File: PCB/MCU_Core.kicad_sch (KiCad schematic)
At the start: 1 part, among them IC2 STM32F407IGT6

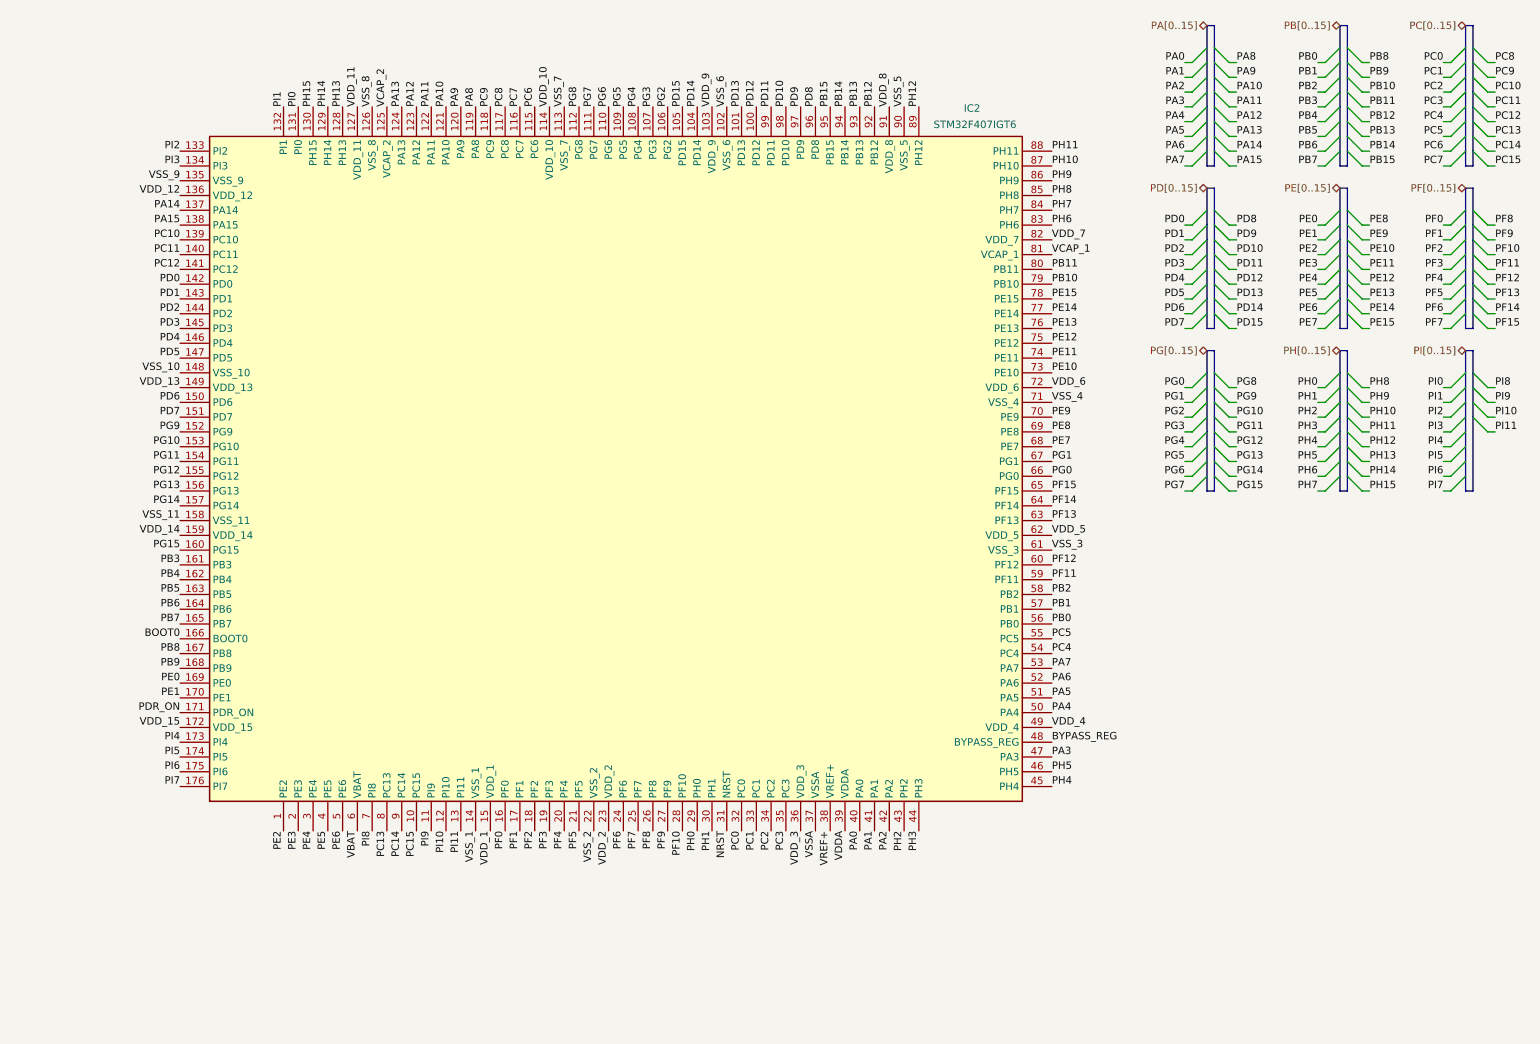
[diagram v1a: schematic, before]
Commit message: ADD supplies to UC
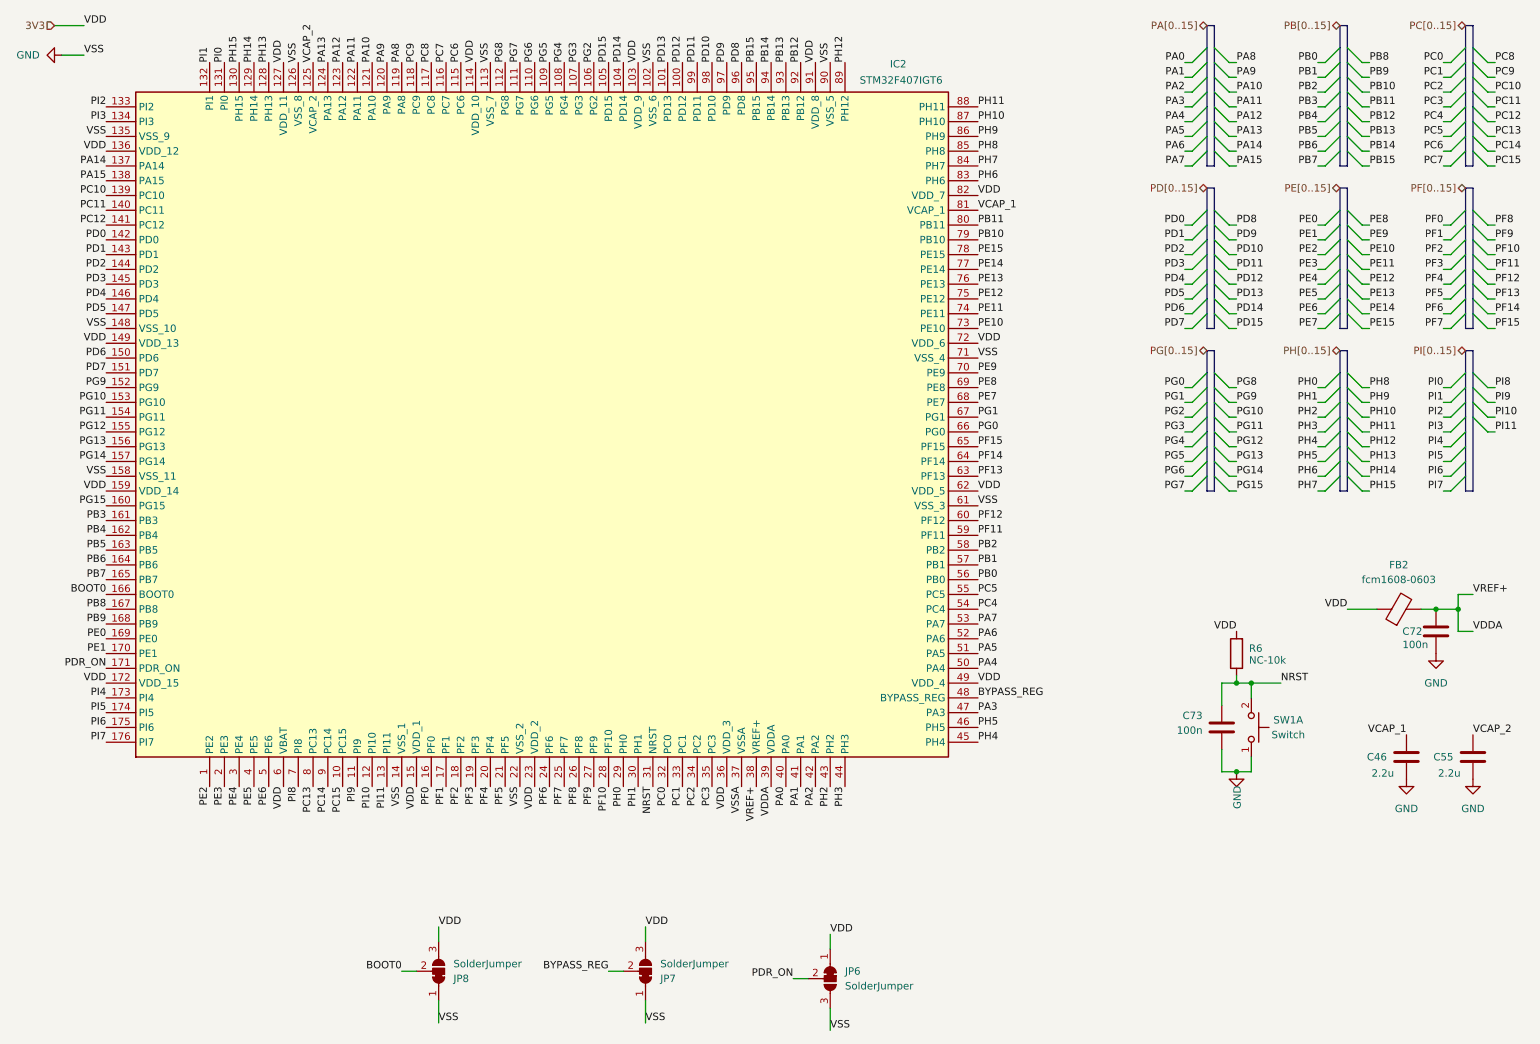
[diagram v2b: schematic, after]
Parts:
- added C46, C55: 2.2u, symbol Device:C
- added C72: 100n, symbol Device:C
- added C73: 100n, Capacitor_SMD:C_0603_1608Metric_Pad1.08x0.95mm_HandSolder, symbol Device:C
- added FB2: fcm1608-0603, symbol Device:FerriteBead
- added JP6, JP7, JP8: SolderJumper, Jumper:SolderJumper-3_P1.3mm_Bridged12_RoundedPad1.0x1.5mm, symbol Jumper:SolderJumper_3_Bridged12
- added R6: NC-10k, Resistor_SMD:R_0603_1608Metric_Pad0.98x0.95mm_HandSolder, symbol Device:R
- added SW1: Switch, SamacSys_Parts:KMR231NGLFS, symbol Switch:SW_Push_Dual_x2
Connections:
- net VDD_1 is gone; now on net 3V3: IC2.15 (VDD_1)
- net VDD_10 is gone; now on net 3V3: IC2.114 (VDD_10)
- net VDD_11 is gone; now on net 3V3: IC2.127 (VDD_11)
- net VDD_12 is gone; now on net 3V3: IC2.136 (VDD_12)
- net VDD_13 is gone; now on net 3V3: IC2.149 (VDD_13)
- net VDD_14 is gone; now on net 3V3: IC2.159 (VDD_14)
- net VDD_15 is gone; now on net 3V3: IC2.172 (VDD_15)
- net VDD_2 is gone; now on net 3V3: IC2.23 (VDD_2)
- net VDD_3 is gone; now on net 3V3: IC2.36 (VDD_3)
- net VDD_4 is gone; now on net 3V3: IC2.49 (VDD_4)
- net VDD_5 is gone; now on net 3V3: IC2.62 (VDD_5)
- net VDD_6 is gone; now on net 3V3: IC2.72 (VDD_6)
- net VDD_7 is gone; now on net 3V3: IC2.82 (VDD_7)
- net VDD_8 is gone; now on net 3V3: IC2.91 (VDD_8)
- net VDD_9 is gone; now on net 3V3: IC2.103 (VDD_9)
- net VREF+ is gone; now on net VDDA: IC2.38 (VREF+)
- net VSS_10 is gone; now on net GND: IC2.148 (VSS_10)
- net VSS_11 is gone; now on net GND: IC2.158 (VSS_11)
- net VSS_2 is gone; now on net GND: IC2.22 (VSS_2)
- net VSS_3 is gone; now on net GND: IC2.61 (VSS_3)
- net VSS_4 is gone; now on net GND: IC2.71 (VSS_4)
- net VSS_5 is gone; now on net GND: IC2.90 (VSS_5)
- net VSS_6 is gone; now on net GND: IC2.102 (VSS_6)
- net VSS_7 is gone; now on net GND: IC2.113 (VSS_7)
- net VSS_8 is gone; now on net GND: IC2.126 (VSS_8)
- net VSS_9 is gone; now on net GND: IC2.135 (VSS_9)
- net BOOT0: now also JP8.2 (C)
- net BYPASS_REG: now also JP7.2 (C)
- net NRST: now also C73.2, R6.1, SW1.2 (D)
- net PDR_ON: now also JP6.2 (C)
- net VCAP_1: now also C46.1
- net VCAP_2: now also C55.1
- net VDDA: now also C72.1, FB2.2
- net VBAT renamed 3V3
- net 3V3: now also FB2.1, JP6.1 (A), JP7.3 (B), JP8.3 (B), R6.2
- net VSS_1 renamed GND
- net GND: now also C46.2, C55.2, C72.2, C73.1, JP6.3 (B), JP7.1 (A), JP8.1 (A), SW1.1 (C)
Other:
- moved on the sheet: IC2

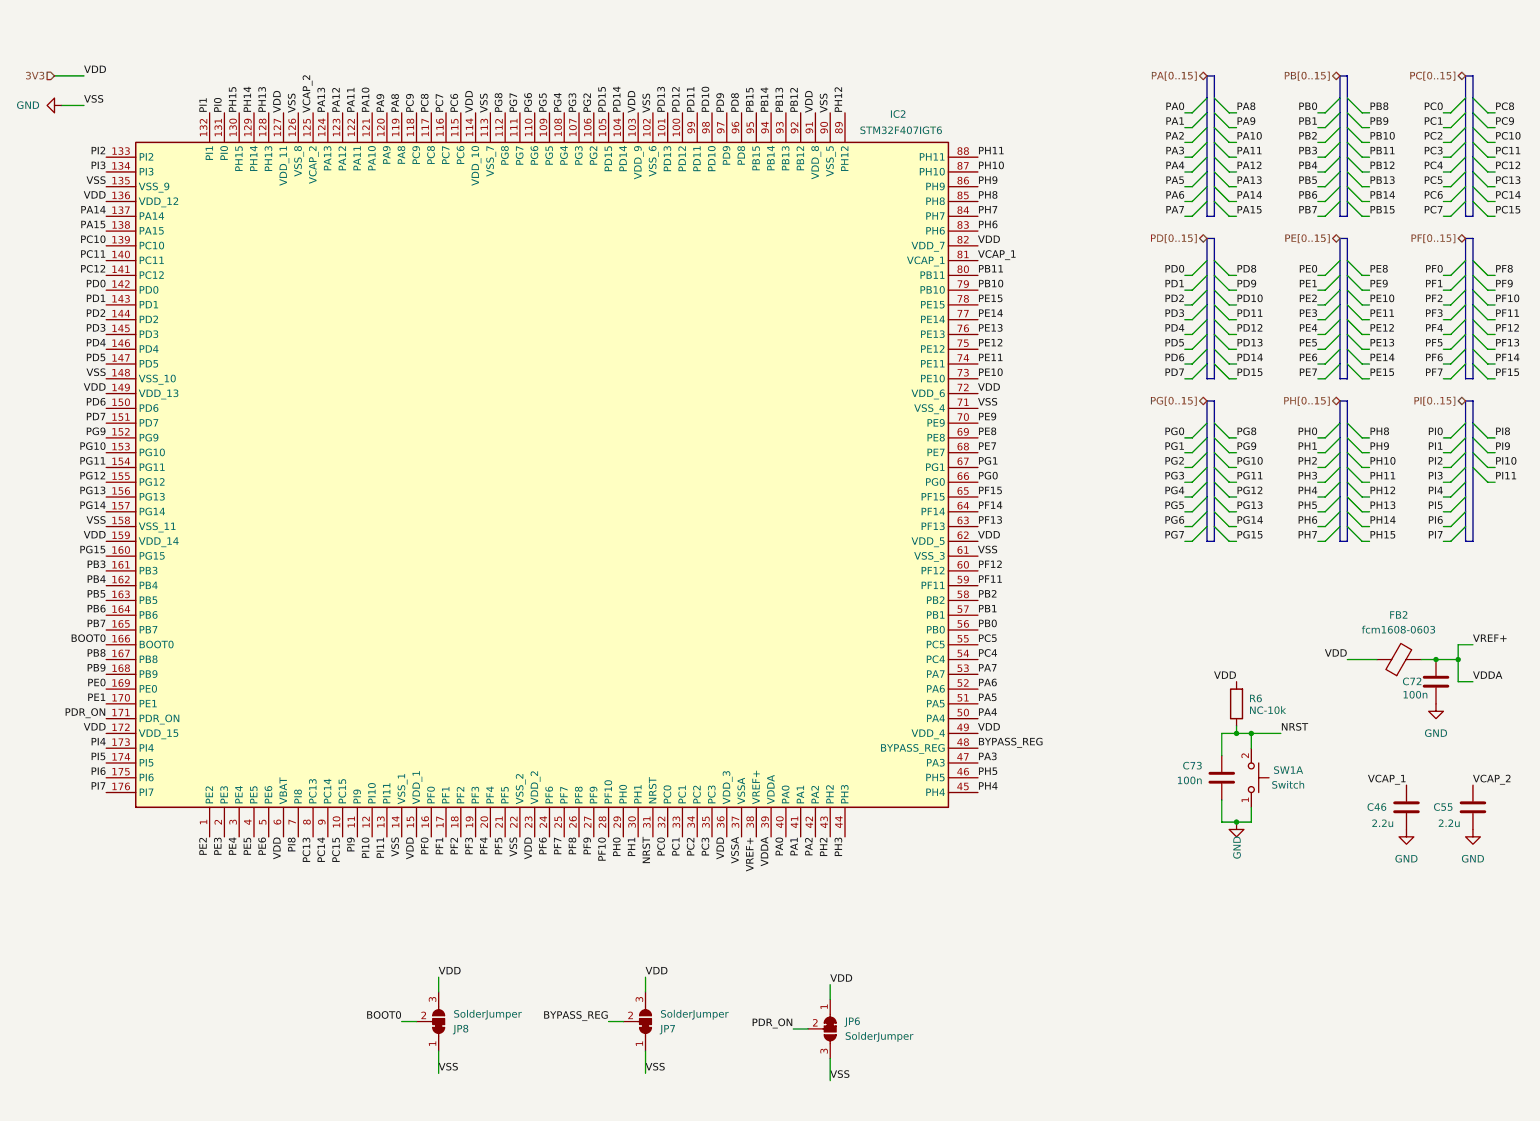
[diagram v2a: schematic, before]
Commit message: Updated MCU sheet
Added decoupling capacitors
Linked Ethernet to MCU
Started Usb linking to MCU
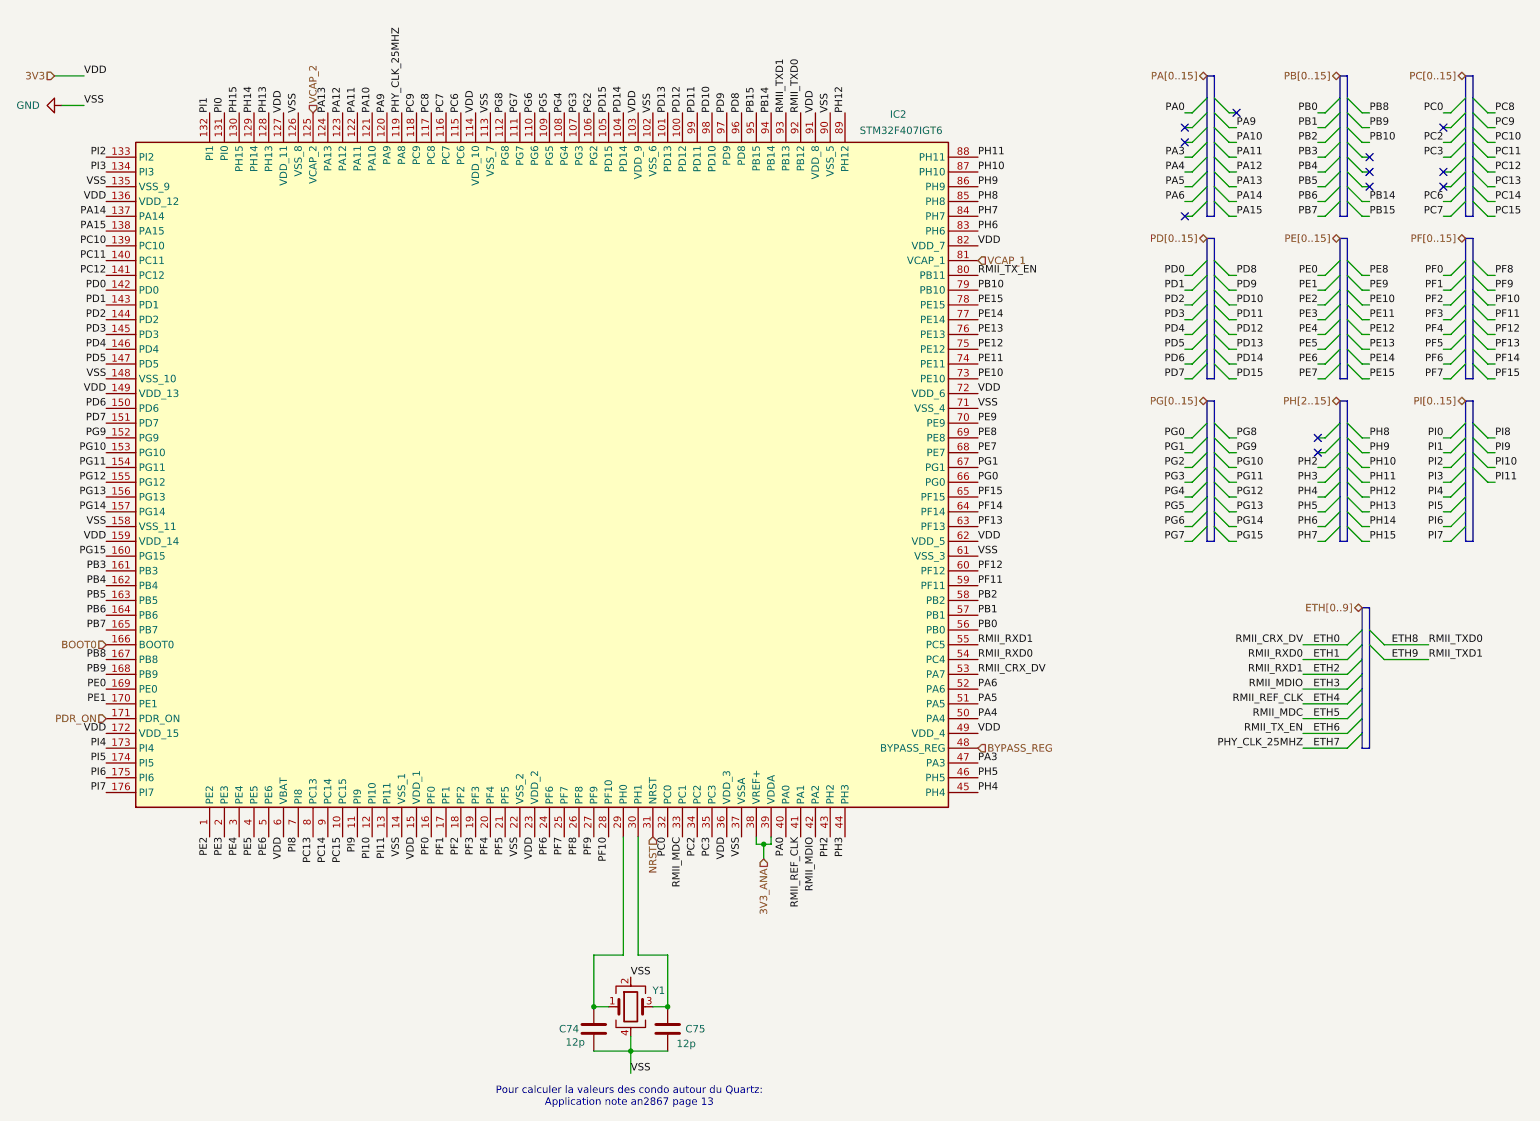
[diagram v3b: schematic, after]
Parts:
- removed C46, C55: 2.2u, symbol Device:C
- removed C72: 100n, symbol Device:C
- removed C73: 100n, Capacitor_SMD:C_0603_1608Metric_Pad1.08x0.95mm_HandSolder, symbol Device:C
- removed FB2: fcm1608-0603, symbol Device:FerriteBead
- removed JP6, JP7, JP8: SolderJumper, Jumper:SolderJumper-3_P1.3mm_Bridged12_RoundedPad1.0x1.5mm, symbol Jumper:SolderJumper_3_Bridged12
- removed R6: NC-10k, Resistor_SMD:R_0603_1608Metric_Pad0.98x0.95mm_HandSolder, symbol Device:R
- removed SW1: Switch, SamacSys_Parts:KMR231NGLFS, symbol Switch:SW_Push_Dual_x2
- added C74, C75: 12p, Capacitor_SMD:C_0603_1608Metric_Pad1.08x0.95mm_HandSolder, symbol Device:C
- added Y1: Crystal_GND24, symbol Device:Crystal_GND24
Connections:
- net VSSA is gone; now on net GND: IC2.37 (VSSA)
- net GND: now also C74.2, C75.2, Y1.2, Y1.4
- net PA1 renamed ETH4
- net PA2 renamed ETH3
- net PA7 renamed ETH0
- net PA8 renamed ETH7
- net PB11 renamed ETH6
- net PB12 renamed ETH8
- net PB13 renamed ETH9
- net PC1 renamed ETH5
- net PC4 renamed ETH1
- net PC5 renamed ETH2
- net PH0: no longer names the net of IC2.29 (PH0)
- net PH0: now also C74.1, Y1.1
- net PH1: no longer names the net of IC2.30 (PH1)
- net PH1: now also C75.1, Y1.3
- net VDDA renamed 3V3_ANA
- no-connect marks 0 -> 12
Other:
- note added: "Pour calculer la valeurs des condo autour du Quartz: Application note an2867 page 13"

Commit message: Updated a lot of stuff:
Added encoders,
Added 5V power supply for actuators
Added 12V power supply for actuators
Renamed sheets to be clearer
Added usb debug
Modify MCU sheet to be A3 format
Linked some pins
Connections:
- net PG11 is gone; now on net ETH6: IC2.154 (PG11)
- net ETH6: no longer IC2.80 (PB11)
- net PA0 renamed SERVO3
- net PA10 renamed RX_UC
- net PA11 renamed D-
- net PA12 renamed D+
- net PA3 renamed CurrentSenseMotor1
- net PA4 renamed CurrentSenseMotor2
- net PA6 renamed ENCODER0
- net PA9 renamed TX_UC
- net PB10 renamed SERVO5
- net PB3 renamed SERVO4
- net PC7 renamed ENCODER1
- net PD12 renamed ENCODER2
- net PD13 renamed ENCODER3
- net PD5 renamed SERVO1
- net PD6 renamed SERVO0
- net PE11 renamed WHEEL3
- net PE13 renamed WHEEL4
- net PE14 renamed WHEEL5
- net PE9 renamed WHEEL2
- new net SERVO6: IC2.80 (PB11)
- no-connect marks 12 -> 30
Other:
- note added: "USB --> PC CALCUL ETHERNET --> PC CALCUL UART1 --> DEBUG"
- moved on the sheet: C74, C75, IC2, Y1
